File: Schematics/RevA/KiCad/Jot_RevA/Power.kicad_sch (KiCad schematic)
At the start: 1 part, among them J2 Battery

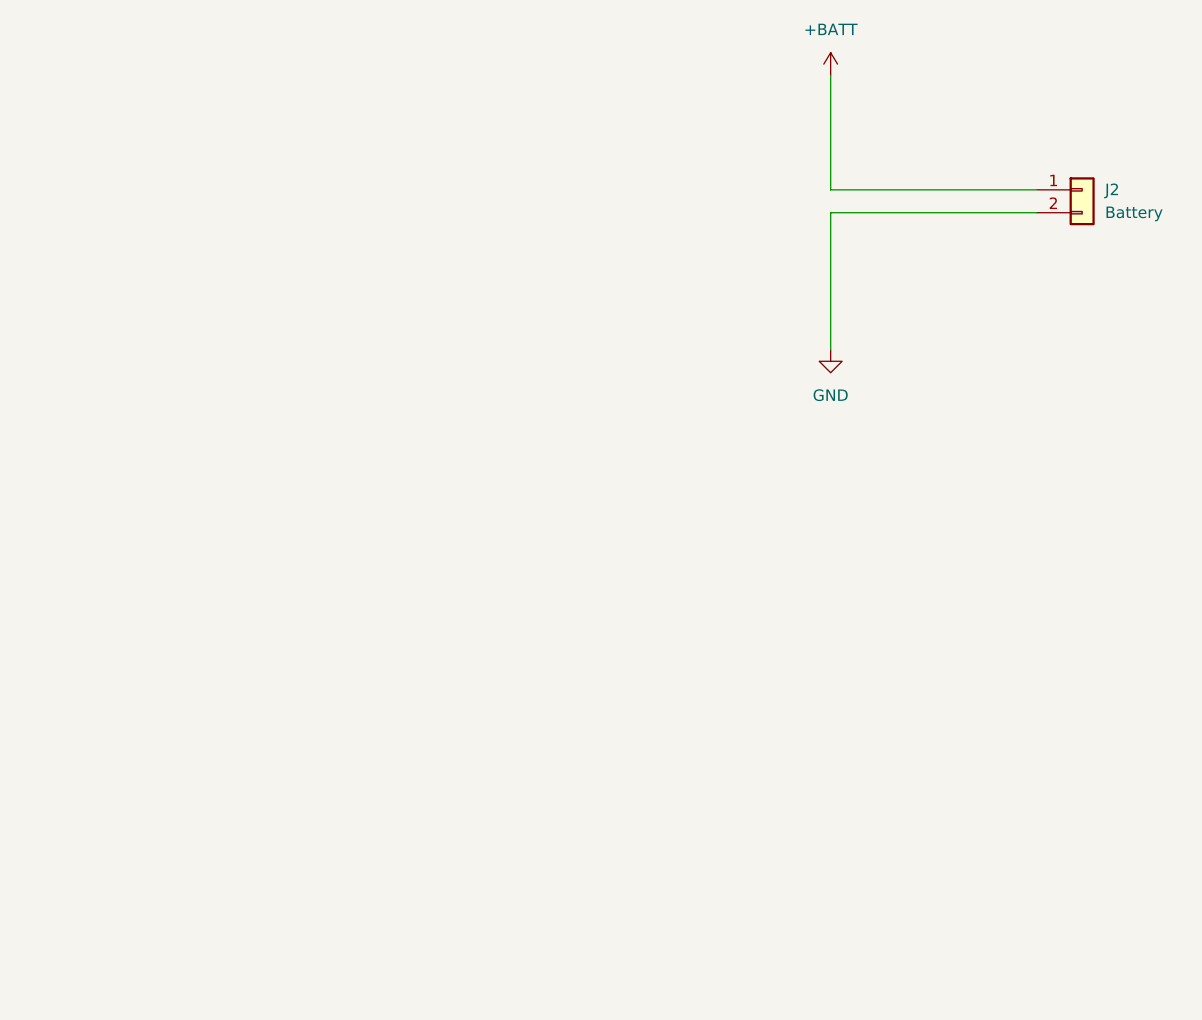
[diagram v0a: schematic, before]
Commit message: KiCad Power: place J1 USB-C, wire VBUS, GND and shield
Co-Authored-By: Claude Opus 5.5 <noreply@anthropic.com>
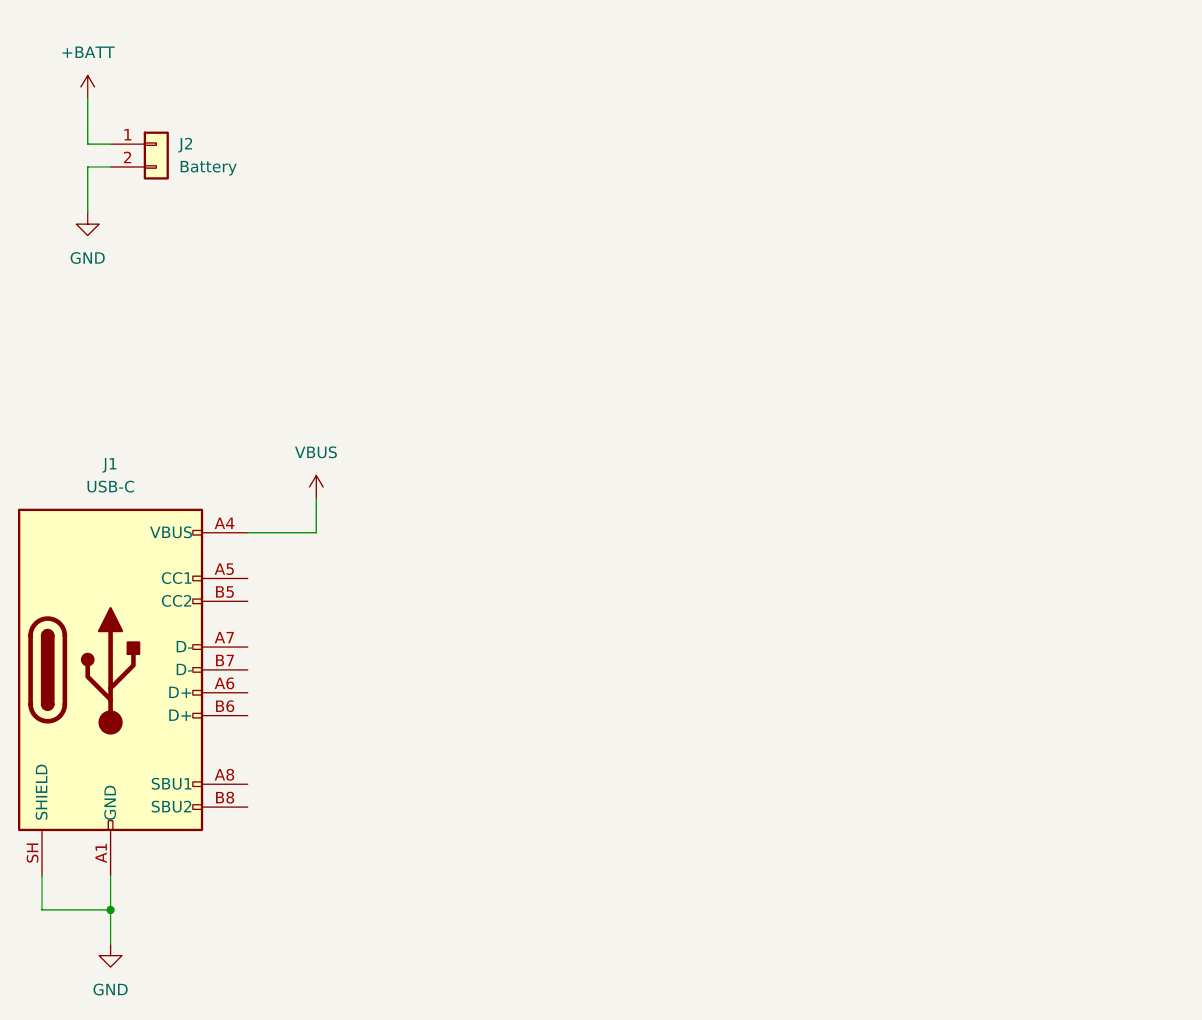
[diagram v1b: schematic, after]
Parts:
- added J1: USB-C, symbol Connector:USB_C_Receptacle_USB2.0_16P
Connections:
- net GND: now also J1.A1 (GND), J1.A12 (GND), J1.B1 (GND), J1.B12 (GND), J1.SH (SHIELD)
- new net VBUS: J1.A4 (VBUS), J1.A9 (VBUS), J1.B4 (VBUS), J1.B9 (VBUS)
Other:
- moved on the sheet: J2

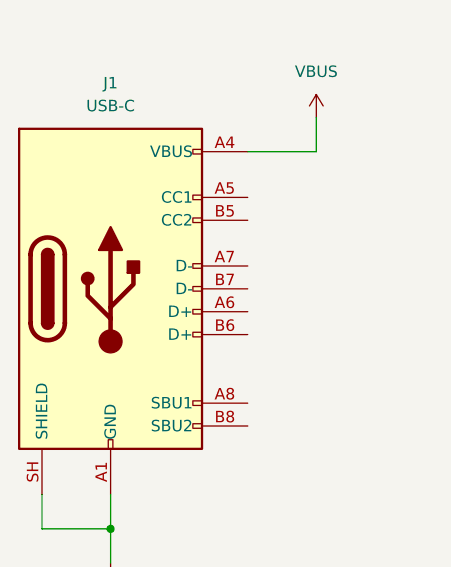
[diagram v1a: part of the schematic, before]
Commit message: KiCad Power: CC1/CC2 pull-downs, local GND symbols, sheet title block
Co-Authored-By: Claude Opus 5.5 <noreply@anthropic.com>
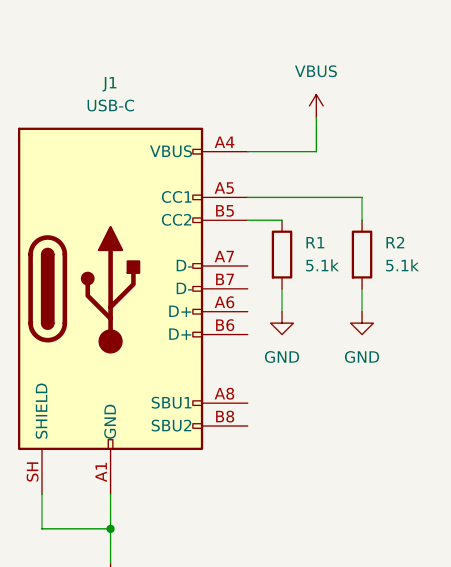
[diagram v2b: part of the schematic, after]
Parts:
- added R1, R2: 5.1k, symbol Device:R
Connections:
- net GND: now also R1.2, R2.2
- net at J1.A5 (CC1): now also R2.1
- net at J1.B5 (CC2): now also R1.1
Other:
- company: (none) -> JC
- title: (none) -> Jot Rev A: Power

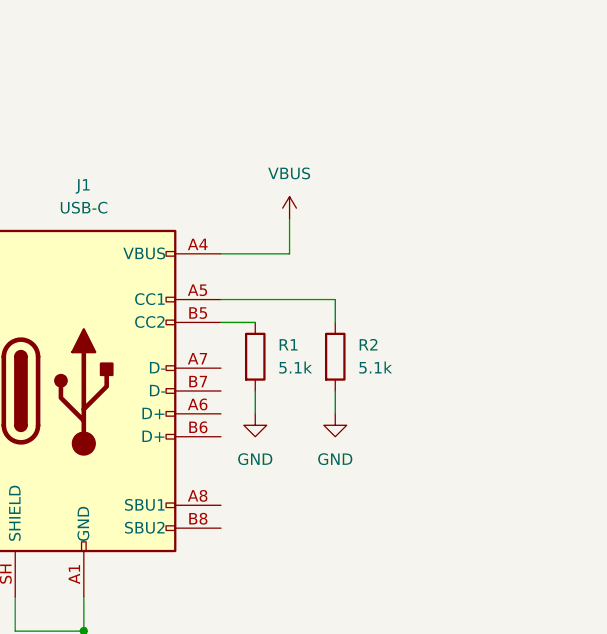
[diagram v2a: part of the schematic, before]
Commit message: KiCad Power: join USB-C D+/D- pairs with USB_DP/USB_DM global labels
Co-Authored-By: Claude Opus 5.5 <noreply@anthropic.com>
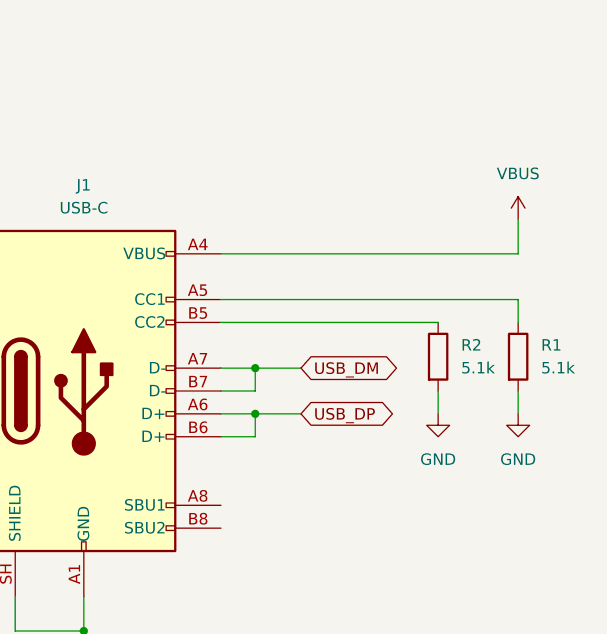
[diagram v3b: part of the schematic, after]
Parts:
- renumbered R2 to R1, R1 to R2
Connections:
- net USB_DP: now reaches J1.A6 (D+)
- net USB_DP: now also J1.B6 (D+)
- net USB_DM: now reaches J1.A7 (D-)
- net USB_DM: now also J1.B7 (D-)
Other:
- moved on the sheet: R1, R2
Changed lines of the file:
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@@
+	)
+	(junction
+		(at 49.53 88.9)
+		(diameter 0)
+		(color 0 0 0 0)
 	)
 	(junction
@@
 		(color 0 0 0 0)
 	)
+	(junction
+		(at 49.53 83.82)
+		(diameter 0)
+		(color 0 0 0 0)
+	)
+	(wire
+		(pts
+			(xy 45.72 86.36) (xy 49.53 86.36)
+		)
+		(stroke
+			(width 0)
+			(type default)
+		)
+	)
+	(wire
+		(pts
+			(xy 45.72 91.44) (xy 49.53 91.44)
+		)
+		(stroke
+			(width 0)
+			(type default)
+		)
+	)
+	(wire
+		(pts
+			(xy 49.53 88.9) (xy 54.61 88.9)
+		)
+		(stroke
+			(width 0)
+			(type default)
+		)
+	)
+	(wire
+		(pts
+			(xy 49.53 83.82) (xy 54.61 83.82)
+		)
+		(stroke
+			(width 0)
+			(type default)
+		)
+	)
 	(wire
 		(pts
@@
 	(wire
 		(pts
-			(xy 45.72 71.12) (xy 53.34 71.12)
+			(xy 45.72 71.12) (xy 78.74 71.12)
 		)
 		(stroke
@@
 	(wire
 		(pts
-			(xy 45.72 76.2) (xy 58.42 76.2)
+			(xy 45.72 76.2) (xy 78.74 76.2)
+		)
+		(stroke
+			(width 0)
+			(type default)
+		)
+	)
+	(wire
+		(pts
+			(xy 45.72 83.82) (xy 49.53 83.82)
 		)
 		(stroke
@@
 	(wire
 		(pts
-			(xy 45.72 78.74) (xy 49.53 78.74)
-		)
-		(stroke
-			(width 0)
-			(type default)
-		)
-	)
-	(wire
-		(pts
-			(xy 53.34 67.31) (xy 53.34 71.12)
-		)
-		(stroke
-			(width 0)
-			(type default)
-		)
-	)
-	(wire
-		(pts
-			(xy 58.42 86.36) (xy 58.42 88.9)
+			(xy 45.72 78.74) (xy 69.85 78.74)
+		)
+		(stroke
+			(width 0)
+			(type default)
+		)
+	)
+	(wire
+		(pts
+			(xy 49.53 83.82) (xy 49.53 86.36)
+		)
+		(stroke
+			(width 0)
+			(type default)
+		)
+	)
+	(wire
+		(pts
+			(xy 78.74 67.31) (xy 78.74 71.12)
+		)
+		(stroke
+			(width 0)
+			(type default)
+		)
+	)
+	(wire
+		(pts
+			(xy 45.72 88.9) (xy 49.53 88.9)
+		)
+		(stroke
+			(width 0)
+			(type default)
+		)
+	)
+	(wire
+		(pts
+			(xy 78.74 86.36) (xy 78.74 88.9)
 		)
 		(stroke
@@
 	(wire
 		(pts
-			(xy 49.53 86.36) (xy 49.53 88.9)
-		)
-		(stroke
-			(width 0)
-			(type default)
-		)
-	)
-	(wire
-		(pts
-			(xy 58.42 78.74) (xy 58.42 76.2)
+			(xy 69.85 86.36) (xy 69.85 88.9)
+		)
+		(stroke
+			(width 0)
+			(type default)
+		)
+	)
+	(wire
+		(pts
+			(xy 78.74 78.74) (xy 78.74 76.2)
+		)
+		(stroke
+			(width 0)
+			(type default)
+		)
+	)
+	(wire
+		(pts
+			(xy 49.53 88.9) (xy 49.53 91.44)
 		)
 		(stroke
@@
 			(width 0)
 			(type default)
+		)
+	)
+	(global_label "USB_DP"
+		(shape bidirectional)
+		(at 54.61 88.9 0)
+		(fields_autoplaced yes)
+		(effects
+			(font
+				(size 1.27 1.27)
+			)
+			(justify left)
+		)
+		(property "Intersheetrefs" "${INTERSHEET_REFS}"
+			(at 66.0241 88.9 0)
+			(hide yes)
+			(show_name no)
+			(do_not_autoplace no)
+			(effects
+				(font
+					(size 1.27 1.27)
+				)
+				(justify left)
+			)
+		)
+	)
+	(global_label "USB_DM"
+		(shape bidirectional)
+		(at 54.61 83.82 0)
+		(fields_autoplaced yes)
+		(effects
+			(font
+				(size 1.27 1.27)
+			)
+			(justify left)
+		)
+		(property "Intersheetrefs" "${INTERSHEET_REFS}"
+			(at 66.2055 83.82 0)
+			(hide yes)
+			(show_name no)
+			(do_not_autoplace no)
+			(effects
+				(font
+					(size 1.27 1.27)
+				)
+				(justify left)
+			)
 		)
 	)
@@
 	(symbol
 		(lib_id "power:VBUS")
-		(at 53.34 67.31 0)
+		(at 78.74 67.31 0)
 		(unit 1)
 		(body_style 1)
@@
 		(fields_autoplaced yes)
 		(property "Reference" "#PWR03"
-			(at 53.34 71.12 0)
+			(at 78.74 71.12 0)
 			(hide yes)
 			(show_name no)
@@
 		)
 		(property "Value" "VBUS"
-			(at 53.34 62.23 0)
+			(at 78.74 62.23 0)
 			(show_name no)
 			(do_not_autoplace no)
@@
 		)
 		(property "Footprint" ""
-			(at 53.34 67.31 0)
+			(at 78.74 67.31 0)
 			(hide yes)
 			(show_name no)
@@
 		)
 		(property "Datasheet" ""
-			(at 53.34 67.31 0)
+			(at 78.74 67.31 0)
 			(hide yes)
 			(show_name no)
@@
 		)
 		(property "Description" "Power symbol creates a global label with name \"VBUS\""
-			(at 53.34 67.31 0)
+			(at 78.74 67.31 0)
 			(hide yes)
 			(show_name no)
@@
 	(symbol
 		(lib_id "Device:R")
-		(at 49.53 82.55 0)
+		(at 69.85 82.55 0)
 		(unit 1)
 		(body_style 1)
@@
 		(dnp no)
 		(fields_autoplaced yes)
-		(property "Reference" "R1"
-			(at 52.07 81.2799 0)
+		(property "Reference" "R2"
+			(at 72.39 81.2799 0)
 			(show_name no)
 			(do_not_autoplace no)
@@
 		)
 		(property "Value" "5.1k"
-			(at 52.07 83.8199 0)
+			(at 72.39 83.8199 0)
 			(show_name no)
 			(do_not_autoplace no)
@@
 		)
 		(property "Footprint" ""
-			(at 47.752 82.55 90)
+			(at 68.072 82.55 90)
 			(hide yes)
 			(show_name no)
@@
 		)
 		(property "Datasheet" ""
-			(at 49.53 82.55 0)
+			(at 69.85 82.55 0)
 			(hide yes)
 			(show_name no)
@@
 		)
 		(property "Description" "Resistor"
-			(at 49.53 82.55 0)
+			(at 69.85 82.55 0)
 			(hide yes)
 			(show_name no)
@@
 			(project "Jot_RevA"
 				(path "/61747270-9f90-47b6-9c50-5ea1f41f259a/3460a3d2-b2cf-48b5-b384-7f5d6528594f"
-					(reference "R1")
+					(reference "R2")
 					(unit 1)
 				)
@@
 	(symbol
 		(lib_id "Device:R")
-		(at 58.42 82.55 0)
+		(at 78.74 82.55 0)
 		(unit 1)
 		(body_style 1)
@@
 		(dnp no)
 		(fields_autoplaced yes)
-		(property "Reference" "R2"
-			(at 60.96 81.2799 0)
+		(property "Reference" "R1"
+			(at 81.28 81.2799 0)
 			(show_name no)
 			(do_not_autoplace no)
@@
 		)
 		(property "Value" "5.1k"
-			(at 60.96 83.8199 0)
+			(at 81.28 83.8199 0)
 			(show_name no)
 			(do_not_autoplace no)
@@
 		)
 		(property "Footprint" ""
-			(at 56.642 82.55 90)
+			(at 76.962 82.55 90)
 			(hide yes)
 			(show_name no)
@@
 		)
 		(property "Datasheet" ""
-			(at 58.42 82.55 0)
+			(at 78.74 82.55 0)
 			(hide yes)
 			(show_name no)
@@
 		)
 		(property "Description" "Resistor"
-			(at 58.42 82.55 0)
+			(at 78.74 82.55 0)
 			(hide yes)
 			(show_name no)
@@
 			(project "Jot_RevA"
 				(path "/61747270-9f90-47b6-9c50-5ea1f41f259a/3460a3d2-b2cf-48b5-b384-7f5d6528594f"
-					(reference "R2")
+					(reference "R1")
 					(unit 1)
 				)
@@
 	(symbol
 		(lib_id "power:GND")
-		(at 58.42 88.9 0)
+		(at 78.74 88.9 0)
 		(unit 1)
 		(body_style 1)
@@
 		(fields_autoplaced yes)
 		(property "Reference" "#PWR06"
-			(at 58.42 95.25 0)
+			(at 78.74 95.25 0)
 			(hide yes)
 			(show_name no)
@@
 		)
 		(property "Value" "GND"
-			(at 58.42 93.98 0)
+			(at 78.74 93.98 0)
 			(show_name no)
 			(do_not_autoplace no)
@@
 		)
 		(property "Footprint" ""
-			(at 58.42 88.9 0)
+			(at 78.74 88.9 0)
 			(hide yes)
 			(show_name no)
@@
 		)
 		(property "Datasheet" ""
-			(at 58.42 88.9 0)
+			(at 78.74 88.9 0)
 			(hide yes)
 			(show_name no)
@@
 		)
 		(property "Description" "Power symbol creates a global label with name \"GND\" , ground"
-			(at 58.42 88.9 0)
+			(at 78.74 88.9 0)
 			(hide yes)
 			(show_name no)
@@
 	(symbol
 		(lib_id "power:GND")
-		(at 49.53 88.9 0)
+		(at 69.85 88.9 0)
 		(unit 1)
 		(body_style 1)
@@
 		(fields_autoplaced yes)
 		(property "Reference" "#PWR05"
-			(at 49.53 95.25 0)
+			(at 69.85 95.25 0)
 			(hide yes)
 			(show_name no)
@@
 		)
 		(property "Value" "GND"
-			(at 49.53 93.98 0)
+			(at 69.85 93.98 0)
 			(show_name no)
 			(do_not_autoplace no)
@@
 		)
 		(property "Footprint" ""
-			(at 49.53 88.9 0)
+			(at 69.85 88.9 0)
 			(hide yes)
 			(show_name no)
@@
 		)
 		(property "Datasheet" ""
-			(at 49.53 88.9 0)
+			(at 69.85 88.9 0)
 			(hide yes)
 			(show_name no)
@@
 		)
 		(property "Description" "Power symbol creates a global label with name \"GND\" , ground"
-			(at 49.53 88.9 0)
-			(hide yes)
-			(show_name no)
+			(at 69.85 88.9 0)
+			(hide yes)
+			(show_name no)
